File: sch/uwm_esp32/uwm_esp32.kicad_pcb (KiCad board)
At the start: 2 copper layers, 85.6 x 54 mm, 25 parts, among them J1 ESP32 Edge Header, J2 DWM Edge Header, SW1 Sleep Button, U1 XIAO_ESP32C3, U2 DWM3000TR13

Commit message: Reroute ESP32 PCB connections
Reworks SPI, GPIO, and 3.3 V routing, updates copper pours, and adjusts default pad dimensions in the KiCad project.
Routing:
- net +3V3: track 139.9 -> 142.9 mm
- net /D9: track 65.0 -> 65.5 mm
- net /SPICLK: track 57.1 -> 57.7 mm
- net GND: vias 133 -> 107

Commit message: Reroute ESP32 board D0 trace
Rework the D0 route and refresh copper fills, including associated ground-via changes. Update the saved KiCad active-layer setting.
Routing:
- net /D0: track 74.1 -> 78.4 mm
- net GND: vias 107 -> 98
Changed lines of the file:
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@@
 	)
 	(segment
-		(start 90.078 91.945928)
-		(end 90.078 75.929072)
+		(start 99.446928 68.227)
+		(end 99.878 67.795928)
+		(width 0.254)
+		(layer "F.Cu")
+		(net "/D0")
+	)
+	(segment
+		(start 106.241819 56.557)
+		(end 106.902 55.896819)
+		(width 0.254)
+		(layer "F.Cu")
+		(net "/D0")
+	)
+	(segment
+		(start 104.125072 56.557)
+		(end 106.241819 56.557)
+		(width 0.254)
+		(layer "F.Cu")
+		(net "/D0")
+	)
+	(segment
+		(start 99.878 60.804072)
+		(end 104.125072 56.557)
+		(width 0.254)
+		(layer "F.Cu")
+		(net "/D0")
+	)
+	(segment
+		(start 109.34 101.275)
+		(end 97.155 101.275)
 		(width 0.254)
 		(layer "F.Cu")
@@
 	)
 	(segment
-		(start 110.338 100.277)
-		(end 98.409072 100.277)
-		(width 0.254)
-		(layer "F.Cu")
-		(net "/D0")
-	)
-	(segment
-		(start 97.780072 68.227)
-		(end 99.446928 68.227)
-		(width 0.254)
-		(layer "F.Cu")
-		(net "/D0")
-	)
-	(segment
-		(start 99.446928 68.227)
-		(end 99.878 67.795928)
+		(start 88.78 92.9)
+		(end 88.78 75.425)
 		(width 0.254)
 		(layer "F.Cu")
@@
 	)
 	(segment
-		(start 104.125072 56.557)
-		(end 106.241819 56.557)
-		(width 0.254)
-		(layer "F.Cu")
-		(net "/D0")
-	)
-	(segment
-		(start 99.878 60.804072)
-		(end 104.125072 56.557)
-		(width 0.254)
-		(layer "F.Cu")
-		(net "/D0")
-	)
-	(segment
-		(start 98.409072 100.277)
-		(end 90.078 91.945928)
-		(width 0.254)
-		(layer "F.Cu")
-		(net "/D0")
-	)
-	(segment
-		(start 90.078 75.929072)
-		(end 97.780072 68.227)
-		(width 0.254)
-		(layer "F.Cu")
-		(net "/D0")
-	)
-	(segment
-		(start 111.515 99.1)
-		(end 110.338 100.277)
+		(start 95.978 68.227)
+		(end 99.446928 68.227)
 		(width 0.254)
 		(layer "F.Cu")
@@
 	)
 	(segment
-		(start 106.241819 56.557)
-		(end 106.902 55.896819)
+		(start 88.78 75.425)
+		(end 95.978 68.227)
+		(width 0.254)
+		(layer "F.Cu")
+		(net "/D0")
+	)
+	(segment
+		(start 97.155 101.275)
+		(end 88.78 92.9)
+		(width 0.254)
+		(layer "F.Cu")
+		(net "/D0")
+	)
+	(segment
+		(start 111.515 99.1)
+		(end 109.34 101.275)
 		(width 0.254)
 		(layer "F.Cu")
@@
 	)
 	(via
-		(at 91.13 78.35)
-		(size 0.6)
-		(drill 0.3)
-		(layers "F.Cu" "B.Cu")
-		(free yes)
-		(net "GND")
-	)
-	(via
-		(at 91.105 88.025)
-		(size 0.6)
-		(drill 0.3)
-		(layers "F.Cu" "B.Cu")
-		(free yes)
-		(net "GND")
-	)
-	(via
 		(at 145.13 74.5)
 		(size 0.6)
@@
 	)
 	(via
-		(at 91.105 89.25)
-		(size 0.6)
-		(drill 0.3)
-		(layers "F.Cu" "B.Cu")
-		(free yes)
-		(net "GND")
-	)
-	(via
 		(at 117.08 67.875)
 		(size 0.6)
@@
 	)
 	(via
-		(at 91.105 84.475)
-		(size 0.6)
-		(drill 0.3)
-		(layers "F.Cu" "B.Cu")
-		(free yes)
-		(net "GND")
-	)
-	(via
 		(at 144.18 74.5)
 		(size 0.6)
@@
 	)
 	(via
-		(at 91.105 89.25)
-		(size 0.6)
-		(drill 0.3)
-		(layers "F.Cu" "B.Cu")
-		(free yes)
-		(net "GND")
-	)
-	(via
 		(at 110.13 59.5)
 		(size 0.6)
@@
 	)
 	(via
-		(at 91.13 79.575)
-		(size 0.6)
-		(drill 0.3)
-		(layers "F.Cu" "B.Cu")
-		(free yes)
-		(net "GND")
-	)
-	(via
 		(at 96.38 83.525)
 		(size 0.6)
@@
 	)
 	(via
-		(at 91.105 84.475)
-		(size 0.6)
-		(drill 0.3)
-		(layers "F.Cu" "B.Cu")
-		(free yes)
-		(net "GND")
-	)
-	(via
 		(at 94.68 95.525)
 		(size 0.6)
@@
 	)
 	(via
-		(at 91.13 79.575)
-		(size 0.6)
-		(drill 0.3)
-		(layers "F.Cu" "B.Cu")
-		(free yes)
-		(net "GND")
-	)
-	(via
 		(at 136.355 66.1)
 		(size 0.6)
@@
 		(size 0.6)
 		(drill 0.3)
-		(layers "F.Cu" "B.Cu")
-		(free yes)
-		(net "GND")
-	)
-	(via
-		(at 91.105 83.25)
-		(size 0.6)
-		(drill 0.3)

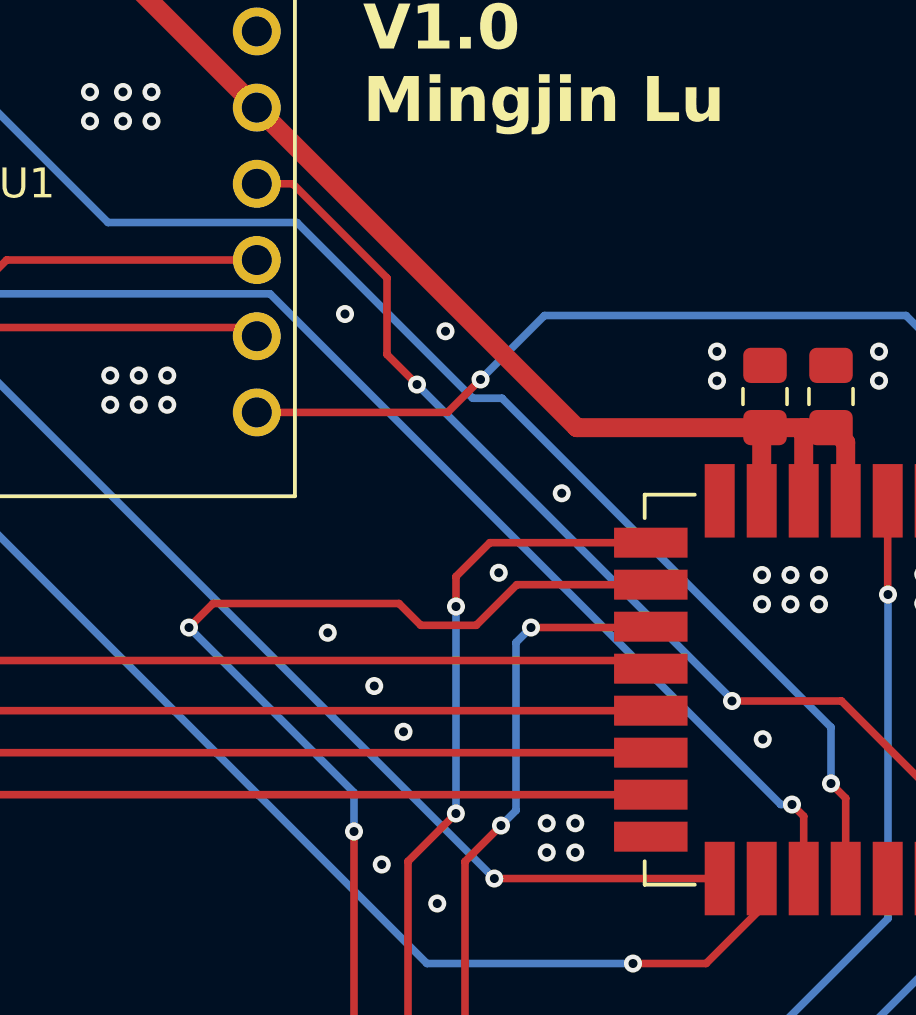
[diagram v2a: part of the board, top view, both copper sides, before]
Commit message: Reroute ESP32 IRQ and SPI traces
Update the IRQ, SPIPHA, and SPIPOL routing, relocate vias, remove two unused GND vias, and refresh the F.Cu zone fills.
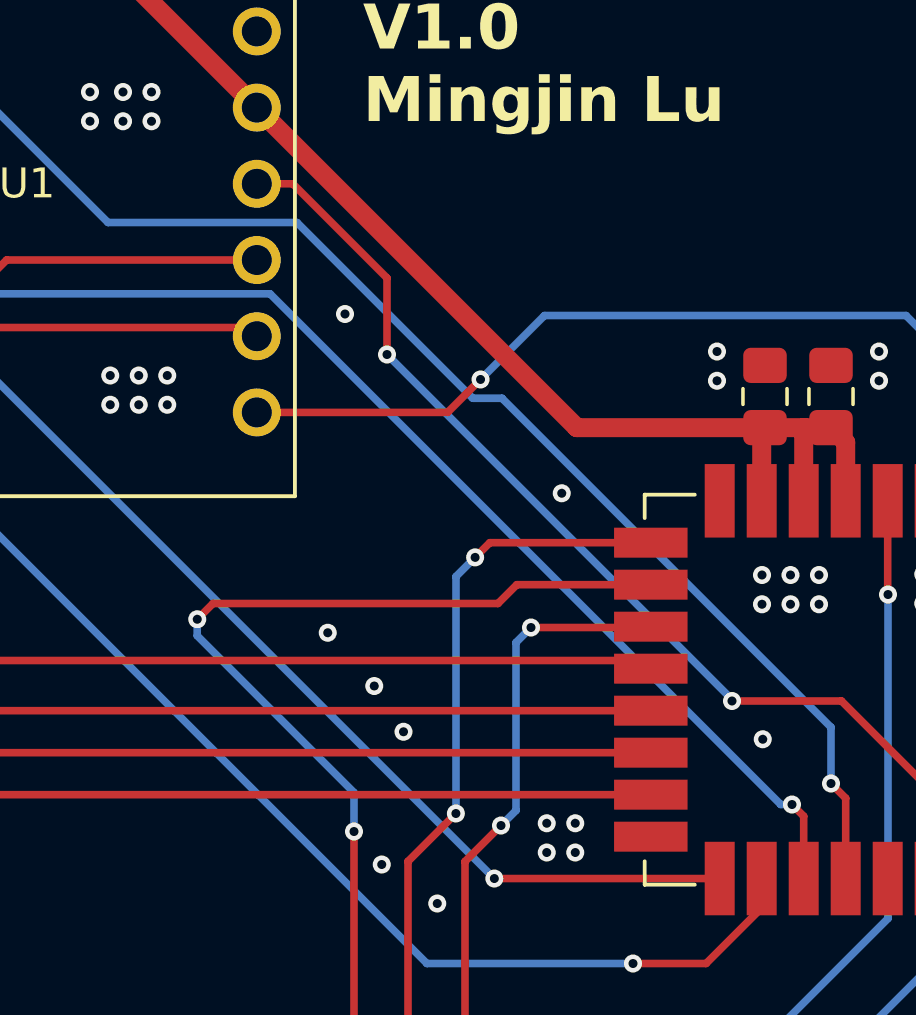
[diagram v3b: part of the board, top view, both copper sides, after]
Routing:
- net /SPIPOL: track 45.1 -> 44.2 mm
- net GND: vias 98 -> 96
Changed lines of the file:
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@@
+	)
+	(segment
+		(start 122.215 60.51)
+		(end 121.015 60.51)
+		(width 0.254)
+		(layer "F.Cu")
+		(net "/IRQ")
 	)
 	(segment
@@
 	)
 	(segment
-		(start 125.355 63.65)
-		(end 125.355 66.2)
-		(width 0.254)
-		(layer "F.Cu")
-		(net "/IRQ")
-	)
-	(segment
-		(start 125.355 66.2)
-		(end 126.355 67.2)
-		(width 0.254)
-		(layer "F.Cu")
-		(net "/IRQ")
-	)
-	(segment
 		(start 140.505 77.75)
 		(end 143.445 80.69)
@@
 	)
 	(segment
+		(start 125.355 66.2)
+		(end 125.355 63.65)
+		(width 0.254)
+		(layer "F.Cu")
+		(net "/IRQ")
+	)
+	(segment
 		(start 121.115 60.51)
 		(end 121.255 60.65)
@@
 	)
 	(segment
+		(start 125.355 63.65)
+		(end 122.215 60.51)
+		(width 0.254)
+		(layer "F.Cu")
+		(net "/IRQ")
+	)
+	(segment
 		(start 143.445 80.69)
 		(end 143.445 83.6675)
@@
 	)
 	(segment
-		(start 121.015 60.51)
-		(end 122.215 60.51)
-		(width 0.254)
-		(layer "F.Cu")
-		(net "/IRQ")
-	)
-	(segment
 		(start 136.855 77.75)
 		(end 140.505 77.75)
@@
 		(net "/IRQ")
 	)
-	(segment
-		(start 122.215 60.51)
-		(end 125.355 63.65)
-		(width 0.254)
-		(layer "F.Cu")
+	(via
+		(at 125.355 66.2)
+		(size 0.6)
+		(drill 0.3)
+		(layers "F.Cu" "B.Cu")
 		(net "/IRQ")
 	)
 	(via
-		(at 126.355 67.2)
+		(at 136.855 77.75)
 		(size 0.6)
 		(drill 0.3)
@@
 		(net "/IRQ")
 	)
-	(via
-		(at 136.855 77.75)
-		(size 0.6)
-		(drill 0.3)
-		(layers "F.Cu" "B.Cu")
+	(segment
+		(start 125.355 66.2)
+		(end 136.855 77.7)
+		(width 0.254)
+		(layer "B.Cu")
 		(net "/IRQ")
 	)
@@
 	)
 	(segment
-		(start 126.355 67.2)
-		(end 136.855 77.7)
-		(width 0.254)
-		(layer "B.Cu")
-		(net "/IRQ")
-	)
-	(segment
 		(start 90.555 56.2)
 		(end 95.655 51.1)
@@
 	)
 	(via
-		(at 127.305 65.425)
-		(size 0.6)
-		(drill 0.3)
-		(layers "F.Cu" "B.Cu")
-		(free yes)
-		(net "GND")
-	)
-	(via
 		(at 98.555 71.4)
 		(size 0.6)
@@
 	(via
 		(at 96.38 83.525)
-		(size 0.6)
-		(drill 0.3)
-		(layers "F.Cu" "B.Cu")
-		(free yes)
-		(net "GND")
-	)
-	(via
-		(at 129.08 73.475)
 		(size 0.6)
 		(drill 0.3)
@@
 	(segment
 		(start 128.7825 72.4725)
-		(end 127.655 73.6)
+		(end 134.15 72.4725)
+		(width 0.254)
+		(layer "F.Cu")
+		(net "/SPIPHA")
+	)
+	(segment
+		(start 128.2925 72.9625)
+		(end 128.7825 72.4725)
 		(width 0.254)
 		(layer "F.Cu")
@@
 	)
 	(segment
-		(start 134.15 72.4725)
-		(end 128.7825 72.4725)
-		(width 0.254)
-		(layer "F.Cu")
-		(net "/SPIPHA")
-	)
-	(segment
 		(start 131.975 99.25)
 		(end 126.055 93.33)
@@
 	)
 	(segment
-		(start 127.655 73.6)
-		(end 127.655 74.6)
-		(width 0.254)
-		(layer "F.Cu")
-		(net "/SPIPHA")
-	)
-	(segment
 		(start 126.055 83.09571)
 		(end 127.651211 81.499499)
@@
 	)
 	(via
-		(at 127.655 74.6)
+		(at 128.2925 72.9625)
 		(size 0.6)
 		(drill 0.3)
@@
 	(segment
 		(start 127.655 81.49571)
-		(end 127.655 74.6)
+		(end 127.651211 81.499499)
 		(width 0.254)
 		(layer "B.Cu")
@@
 	)
 	(segment
-		(start 127.651211 81.499499)
+		(start 128.2925 72.9625)
+		(end 127.655 73.6)
+		(width 0.254)
+		(layer "B.Cu")
+		(net "/SPIPHA")
+	)
+	(segment
+		(start 127.655 73.6)
 		(end 127.655 81.49571)
 		(width 0.254)
@@
 	)
 	(segment
-		(start 126.482 75.227)
-		(end 125.755 74.5)
-		(width 0.254)
-		(layer "F.Cu")
-		(net "/SPIPOL")
-	)
-	(segment
-		(start 128.328 75.227)
-		(end 126.482 75.227)
+		(start 119.03 75.025)
+		(end 119.555 74.5)
 		(width 0.254)
 		(layer "F.Cu")
@@
 	)
 	(segment
-		(start 134.15 73.8725)
+		(start 129.6825 73.8725)
+		(end 134.15 73.8725)
+		(width 0.254)
+		(layer "F.Cu")
+		(net "/SPIPOL")
+	)
+	(segment
+		(start 129.055 74.5)
 		(end 129.6825 73.8725)
 		(width 0.254)
@@
 	(segment
 		(start 119.555 74.5)
-		(end 118.755 75.3)
+		(end 129.055 74.5)
 		(width 0.254)
 		(layer "F.Cu")
 		(net "/SPIPOL")
 	)
-	(segment
-		(start 129.6825 73.8725)
-		(end 128.328 75.227)
-		(width 0.254)
-		(layer "F.Cu")
+	(via
+		(at 124.255 82.1)
+		(size 0.6)
+		(drill 0.3)
+		(layers "F.Cu" "B.Cu")
 		(net "/SPIPOL")
 	)
-	(segment
-		(start 125.755 74.5)
-		(end 119.555 74.5)
-		(width 0.254)
-		(layer "F.Cu")
+	(via
+		(at 119.03 75.025)
+		(size 0.6)
+		(drill 0.3)
+		(layers "F.Cu" "B.Cu")
 		(net "/SPIPOL")
 	)
-	(via
-		(at 124.255 82.1)
-		(size 0.6)
-		(drill 0.3)
-		(layers "F.Cu" "B.Cu")
+	(segment
+		(start 124.255 80.8)
+		(end 124.255 82.1)
+		(width 0.254)
+		(layer "B.Cu")
 		(net "/SPIPOL")
 	)
-	(via
-		(at 118.755 75.3)
-		(size 0.6)
-		(drill 0.3)
-		(layers "F.Cu" "B.Cu")
-		(net "/SPIPOL")
-	)
-	(segment
-		(start 118.755 75.3)
-		(end 124.255 80.8)
+	(segment
+		(start 119.03 75.025)
+		(end 119.03 75.575)
 		(width 0.254)
 		(layer "B.Cu")
@@
 	)
 	(segment
-		(start 124.255 80.8)
-		(end 124.255 82)
-		(width 0.254)
-		(layer "B.Cu")
-		(net "/SPIPOL")
-	)
-	(segment
-		(start 124.255 82)
-		(end 124.255 82.1)
-		(width 0.254)
-		(layer "B.Cu")
+		(start 119.03 75.575)
+		(end 124.255 80.8)
+		(width 0.254)
+		(layer "B.Cu")
